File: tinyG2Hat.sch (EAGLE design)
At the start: 5 parts

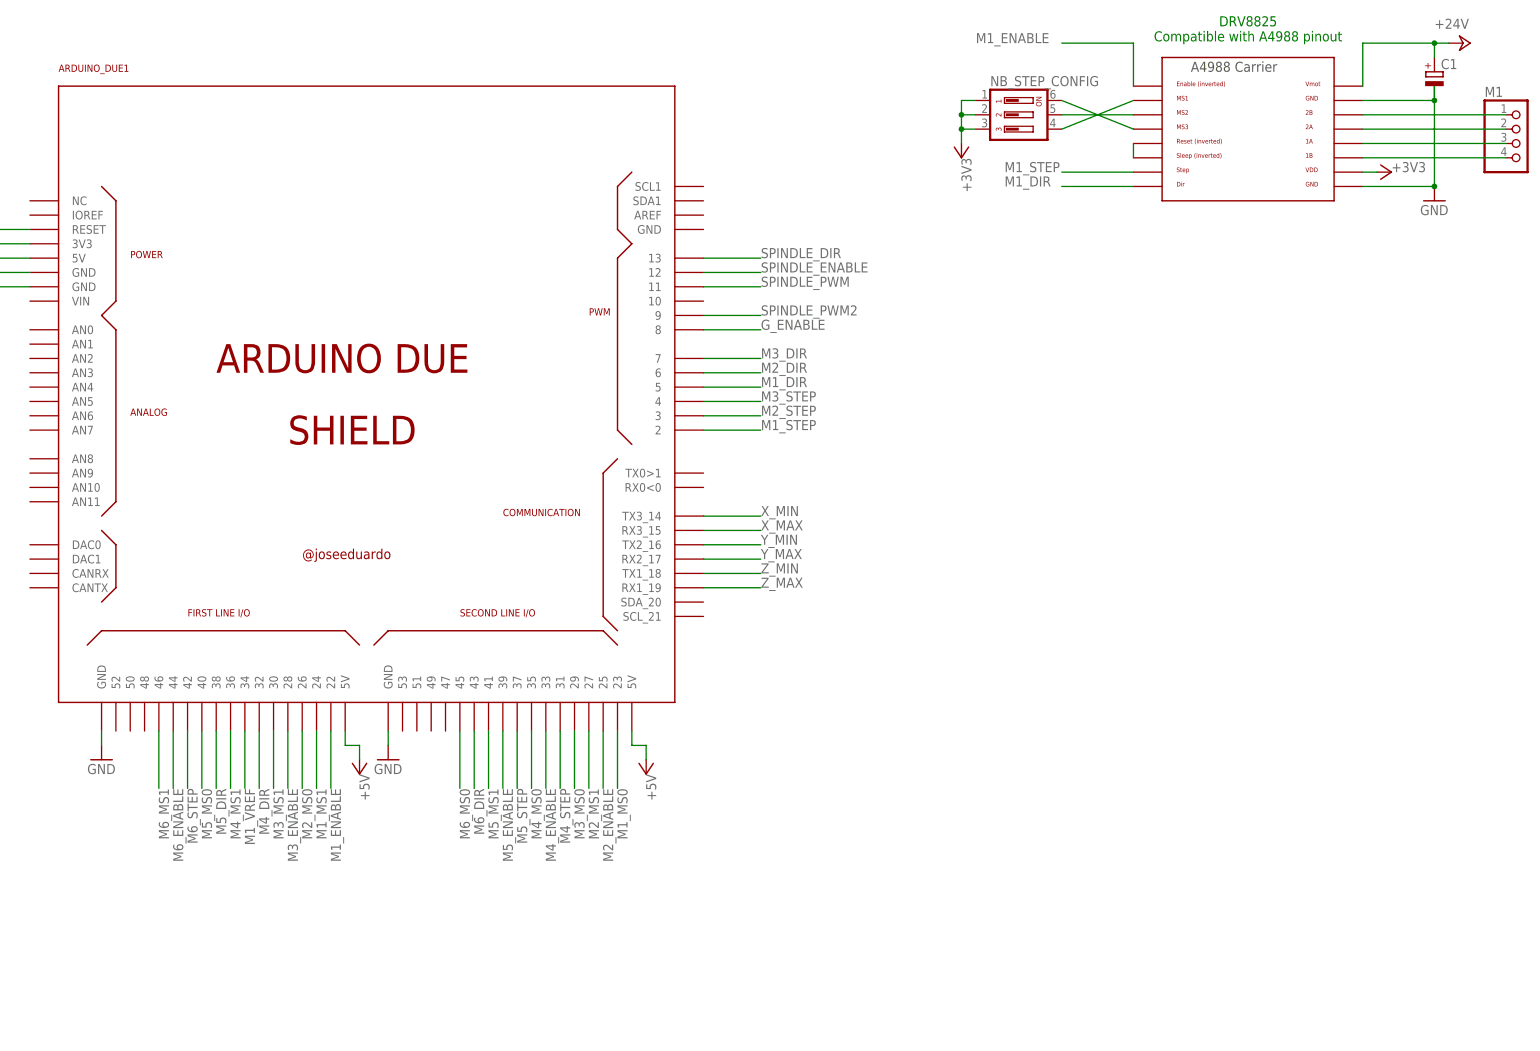
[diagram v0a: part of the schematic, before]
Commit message: 6 moteurs placés dans le schematic
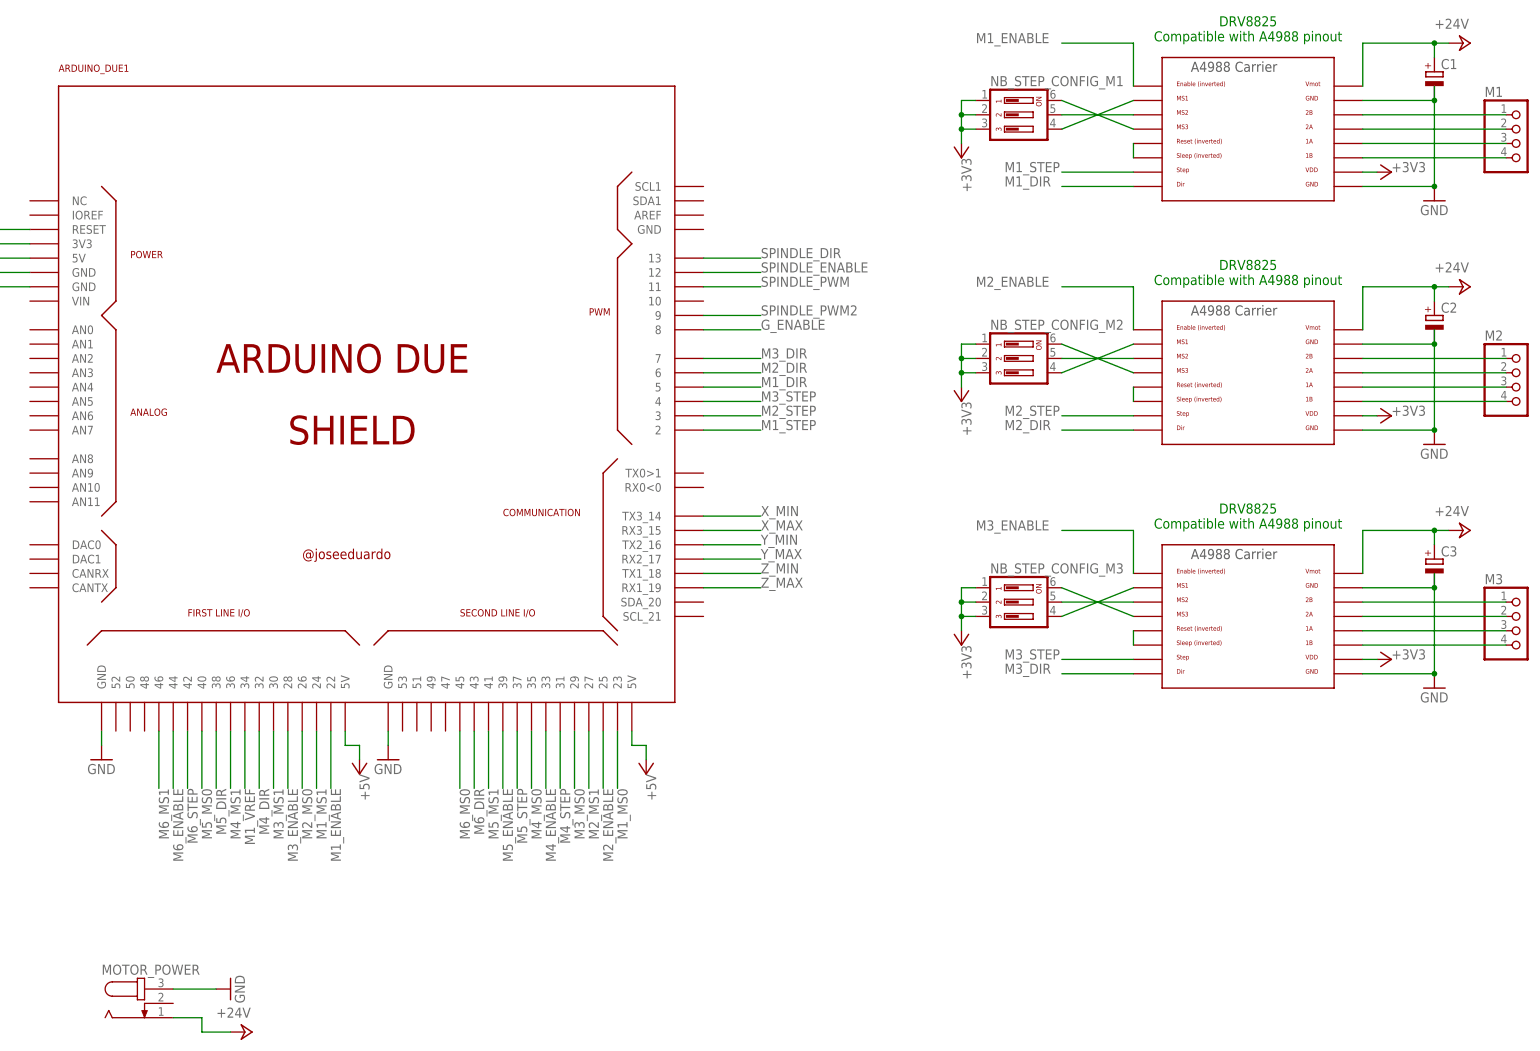
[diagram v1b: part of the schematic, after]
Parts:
- added C2, C3: (no value), rcl:CPOL-EUE3.5-8
- added M2, M3: (no value), pinhead:PINHD-1X4
- added MOTOR_POWER: (no value), RepRapjr:RAPC7120
- added NB_STEP_CONFIG_M2, NB_STEP_CONFIG_M3: (no value), switch-dil:DIP03YL
- added U$2, U$3: A4988BREAKOUT, RepRapjr:A4988BREAKOUT
- C1: device rcl:CPOL-EUE5-10.5 -> rcl:CPOL-EUE3.5-8
- renumbered NB_STEP_CONFIG to NB_STEP_CONFIG_M1
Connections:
- new net N$10: U$2.RST, U$2.SLEEP
- new net N$11: M2.1, U$2.2B
- new net N$12: M2.2, U$2.2A
- new net N$13: M2.3, U$2.1A
- new net N$14: M2.4, U$2.1B
- new net N$15: NB_STEP_CONFIG_M2.6, U$2.MS3
- new net N$16: NB_STEP_CONFIG_M2.4, U$2.MS1
- new net N$17: NB_STEP_CONFIG_M3.5, U$3.MS2
- new net N$18: U$3.RST, U$3.SLEEP
- new net N$19: M3.1, U$3.2B
- new net N$20: M3.2, U$3.2A
- new net N$21: M3.3, U$3.1A
- new net N$22: M3.4, U$3.1B
- new net N$23: NB_STEP_CONFIG_M3.6, U$3.MS3
- new net N$24: NB_STEP_CONFIG_M3.4, U$3.MS1
- new net N$9: NB_STEP_CONFIG_M2.5, U$2.MS2
- net +24V: now also C2.+, C3.+, MOTOR_POWER.1, U$2.VMOT, U$3.VMOT
- net +3V3: now also NB_STEP_CONFIG_M2.1, NB_STEP_CONFIG_M2.2, NB_STEP_CONFIG_M2.3, NB_STEP_CONFIG_M3.1, NB_STEP_CONFIG_M3.2, NB_STEP_CONFIG_M3.3, U$2.VDD, U$3.VDD
- net GND: now also C2.-, C3.-, MOTOR_POWER.3, U$2.GND@0, U$2.GND@1, U$3.GND@0, U$3.GND@1
- net M2_DIR: now also U$2.DIR
- net M2_ENABLE: now also U$2.EN
- net M2_STEP: now also U$2.STEP
- net M3_DIR: now also U$3.DIR
- net M3_ENABLE: now also U$3.EN
- net M3_STEP: now also U$3.STEP

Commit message: Ajout des entrée capteurs fin course et sortie spindle dans le schematic
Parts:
- added C4, C5, C6: (no value), rcl:CPOL-EUE3.5-8
- added M4, M5, M6: (no value), pinhead:PINHD-1X4
- added NB_STEP_CONFIG_M4, NB_STEP_CONFIG_M5, NB_STEP_CONFIG_M6: (no value), switch-dil:DIP03YL
- added S2: (no value), switch-dil:DP08
- added SPINDLE_OUTPUTS: (no value), con-lstb:MA05-2
- added SV1: (no value), con-lstb:MA04-2
- added U$4, U$5, U$6: A4988BREAKOUT, RepRapjr:A4988BREAKOUT
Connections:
- new net COOLANT_ON: ARDUINO_DUE1.AN3, SPINDLE_OUTPUTS.1
- new net CY_START: ARDUINO_DUE1.AN2
- new net EEED_HOLD: ARDUINO_DUE1.AN1
- new net E_STOP: ARDUINO_DUE1.AN4, S2.10
- new net H_INTERLCK: ARDUINO_DUE1.AN6, S2.9
- new net N$25: NB_STEP_CONFIG_M4.5, U$4.MS2
- new net N$26: U$4.RST, U$4.SLEEP
- new net N$27: M4.1, U$4.2B
- new net N$28: M4.2, U$4.2A
- new net N$29: M4.3, U$4.1A
- new net N$30: M4.4, U$4.1B
- new net N$31: NB_STEP_CONFIG_M4.6, U$4.MS3
- new net N$32: NB_STEP_CONFIG_M4.4, U$4.MS1
- new net N$33: NB_STEP_CONFIG_M5.5, U$5.MS2
- new net N$34: U$5.RST, U$5.SLEEP
- new net N$35: M5.1, U$5.2B
- new net N$36: M5.2, U$5.2A
- new net N$37: M5.3, U$5.1A
- new net N$38: M5.4, U$5.1B
- new net N$39: NB_STEP_CONFIG_M5.6, U$5.MS3
- new net N$40: NB_STEP_CONFIG_M5.4, U$5.MS1
- new net N$41: NB_STEP_CONFIG_M6.5, U$6.MS2
- new net N$42: U$6.RST, U$6.SLEEP
- new net N$43: M6.1, U$6.2B
- new net N$44: M6.2, U$6.2A
- new net N$45: M6.3, U$6.1A
- new net N$46: M6.4, U$6.1B
- new net N$47: NB_STEP_CONFIG_M6.6, U$6.MS3
- new net N$48: NB_STEP_CONFIG_M6.4, U$6.MS1
- new net N$49: S2.1, S2.2, SV1.7
- new net N$51: S2.3, S2.4, SV1.5
- new net N$53: S2.5, S2.6, SV1.3
- new net N$55: S2.7, S2.8, SV1.1
- new net SOFT_RESET: ARDUINO_DUE1.AN0
- net +24V: now also C4.+, C5.+, C6.+, U$4.VMOT, U$5.VMOT, U$6.VMOT
- net +3V3: now also NB_STEP_CONFIG_M4.1, NB_STEP_CONFIG_M4.2, NB_STEP_CONFIG_M4.3, NB_STEP_CONFIG_M5.1, NB_STEP_CONFIG_M5.2, NB_STEP_CONFIG_M5.3, NB_STEP_CONFIG_M6.1, NB_STEP_CONFIG_M6.2, NB_STEP_CONFIG_M6.3, U$4.VDD, U$5.VDD, U$6.VDD
- net GND: now also C4.-, C5.-, C6.-, SPINDLE_OUTPUTS.10, SPINDLE_OUTPUTS.2, SPINDLE_OUTPUTS.4, SPINDLE_OUTPUTS.6, SPINDLE_OUTPUTS.8, SV1.2, SV1.4, SV1.6, SV1.8, U$4.GND@0, U$4.GND@1, U$5.GND@0, U$5.GND@1, U$6.GND@0, U$6.GND@1
- net M4_DIR: now also U$4.DIR
- net M4_ENABLE: now also U$4.EN
- net M4_STEP: now also U$4.STEP
- net M5_DIR: now also U$5.DIR
- net M5_ENABLE: now also U$5.EN
- net M5_STEP: now also U$5.STEP
- net M6_DIR: now also U$6.DIR
- net M6_ENABLE: now also U$6.EN
- net M6_STEP: now also U$6.STEP
- net SPINDLE_DIR: now also SPINDLE_OUTPUTS.7
- net SPINDLE_ENABLE: now also SPINDLE_OUTPUTS.9
- net SPINDLE_PWM: now also SPINDLE_OUTPUTS.5
- net SPINDLE_PWM2: now also SPINDLE_OUTPUTS.3
- net X_MAX: now also S2.15
- net X_MIN: now also S2.16
- net Y_MAX: now also S2.13
- net Y_MIN: now also S2.14
- net Z_MAX: now also S2.11
- net Z_MIN: now also S2.12

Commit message: Ajout des commandes manuelles
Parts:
- added CONTROL_SWITCHES_INPUTS: (no value), pinhead:PINHD-2X5
- added RESET_SWITCH: (no value), RepRapjr:10-XX-RPAD
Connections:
- removed net EEED_HOLD: ARDUINO_DUE1.AN1
- new net FEED_HOLD: ARDUINO_DUE1.AN1, CONTROL_SWITCHES_INPUTS.4
- new net N$50: CONTROL_SWITCHES_INPUTS.10, RESET_SWITCH.P
- net CY_START: now also CONTROL_SWITCHES_INPUTS.6
- net E_STOP: now also CONTROL_SWITCHES_INPUTS.8, S2.15; no longer S2.10
- net GND: now also CONTROL_SWITCHES_INPUTS.1, CONTROL_SWITCHES_INPUTS.3, CONTROL_SWITCHES_INPUTS.5, CONTROL_SWITCHES_INPUTS.7, CONTROL_SWITCHES_INPUTS.9, RESET_SWITCH.GND1, RESET_SWITCH.GND2
- net H_INTERLCK: now also S2.16; no longer S2.9
- net RESET: now also RESET_SWITCH.S
- net SOFT_RESET: now also CONTROL_SWITCHES_INPUTS.2
- net X_MAX: now also S2.10; no longer S2.15
- net X_MIN: now also S2.9; no longer S2.16
- net Y_MAX: now also S2.12; no longer S2.13
- net Y_MIN: now also S2.11; no longer S2.14
- net Z_MAX: now also S2.14; no longer S2.11
- net Z_MIN: now also S2.13; no longer S2.12
